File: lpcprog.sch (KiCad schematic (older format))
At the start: 32 parts, among them IC1 LPC111X/102, P1 CONN_6, P2 CONN_6, P3 CONN_6, P4 CONN_4, P5 CONN_4, P6 CONN_8, P7 CONN_5, SW1 SW_PUSH, U1 MICROUSB, U2 FT232RL, U3 74LS125, U4 TLV1117-SOT223, X1 CONN_4

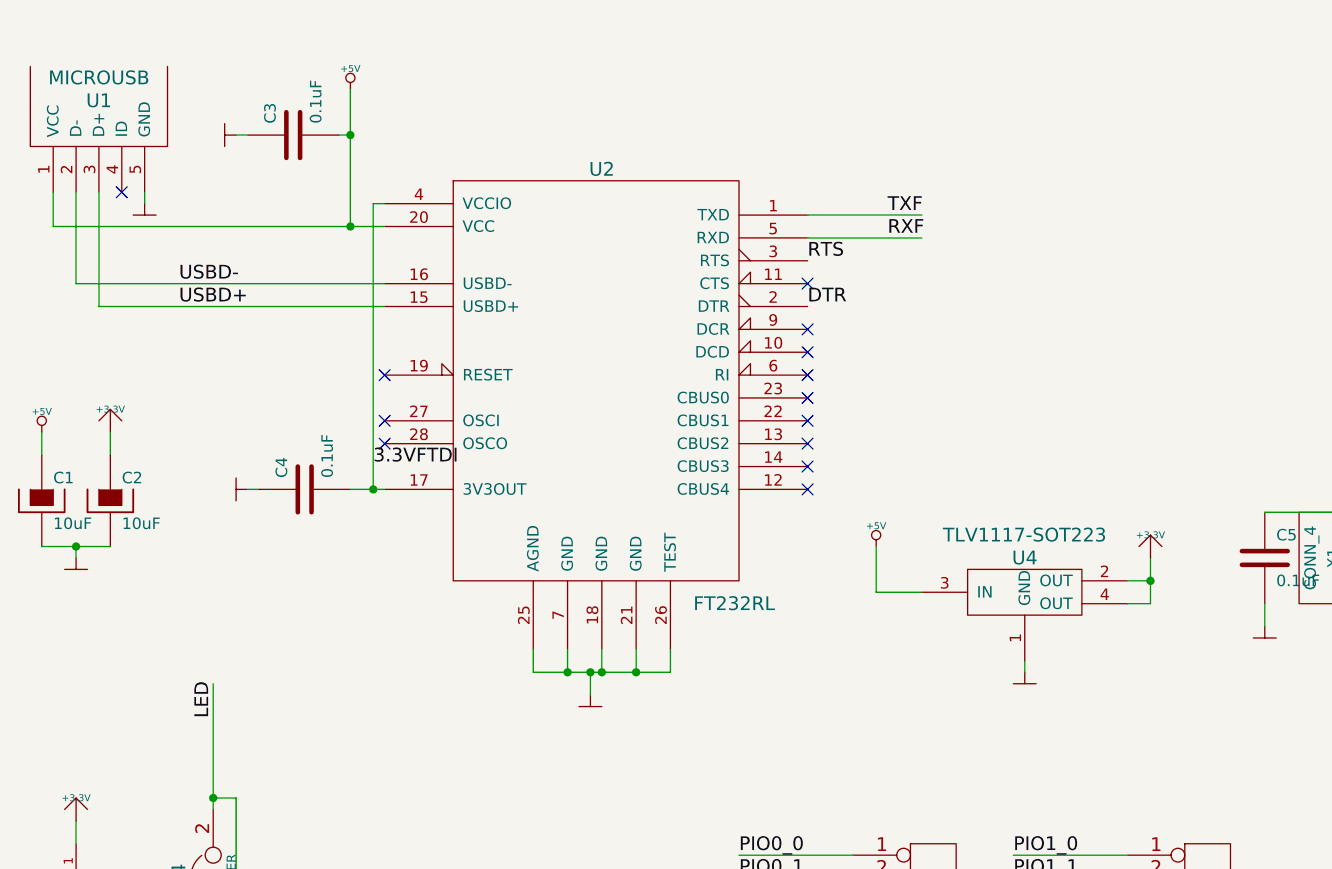
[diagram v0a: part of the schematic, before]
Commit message: LPC1114FN28 (LPC1114 Cortex-M0) programmer board
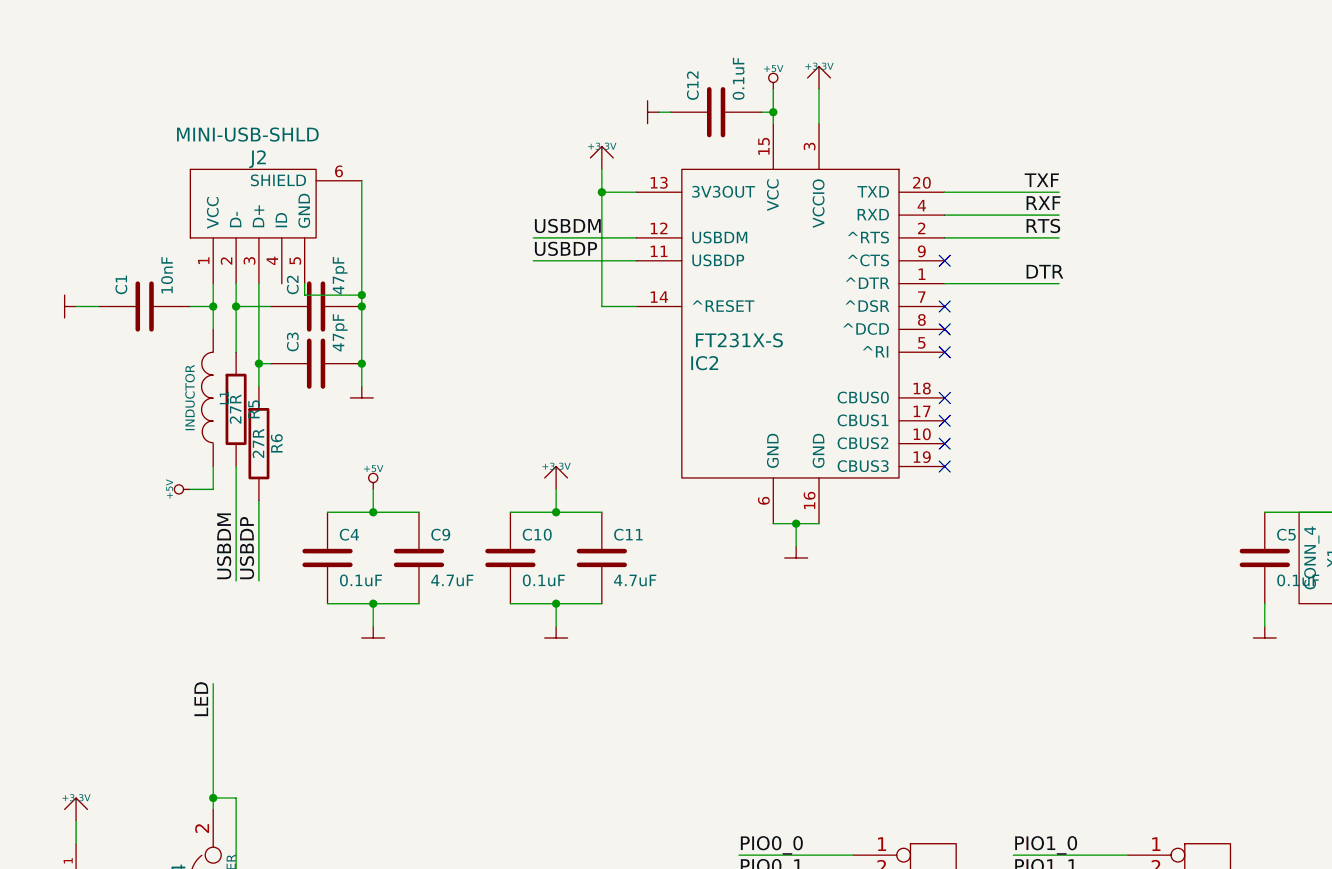
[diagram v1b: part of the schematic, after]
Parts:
- removed C1, C2: 10uF, symbol CP
- removed U1: MICROUSB, symbol MICROUSB
- removed U2: FT232RL, symbol FT232RL
- removed U4: TLV1117-SOT223, symbol TLV1117-SOT223
- added C1: 10nF, symbol C
- added C10, C12: 0.1uF, symbol C
- added C11, C9: 4.7uF, symbol C
- added C2: 47pF, symbol C
- added IC2: FT231X-S, symbol FT231X-S
- added J2: MINI-USB-SHLD, symbol MINI-USB-SHLD
- added L1: INDUCTOR, symbol INDUCTOR
- added R5, R6: 27R, symbol R
- C3: value 0.1uF -> 47pF
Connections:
- net labels added: USBDM, USBDP
- net labels removed: 3.3VFTDI, USBD+, USBD-
- wire segments 151 -> 155
- no-connect marks 18 -> 13
